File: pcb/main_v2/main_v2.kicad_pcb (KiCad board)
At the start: 4 copper layers, 68.5 x 135.2 mm, 97 parts, among them IC201 AP22811AW5-7, IC301 SE2576L-R, IC302 RMS-30+, IC401 RMS-30+, IC402 HMC374, IC501 SPF5043Z, IC502 PD0922J5050S2HF, IC503 SPF5043Z, J102 Conn_02x06_Odd_Even, J201 USB_A, J301 Conn_Coaxial, J302 Conn_Coaxial, J401 Conn_Coaxial, J402 Conn_Coaxial, SW201 SW_DIP_x01, U201 LT3042xMSE, U501 XMB0220K1-50100G, Y501 ASGTX-P-1.500GHZ-1

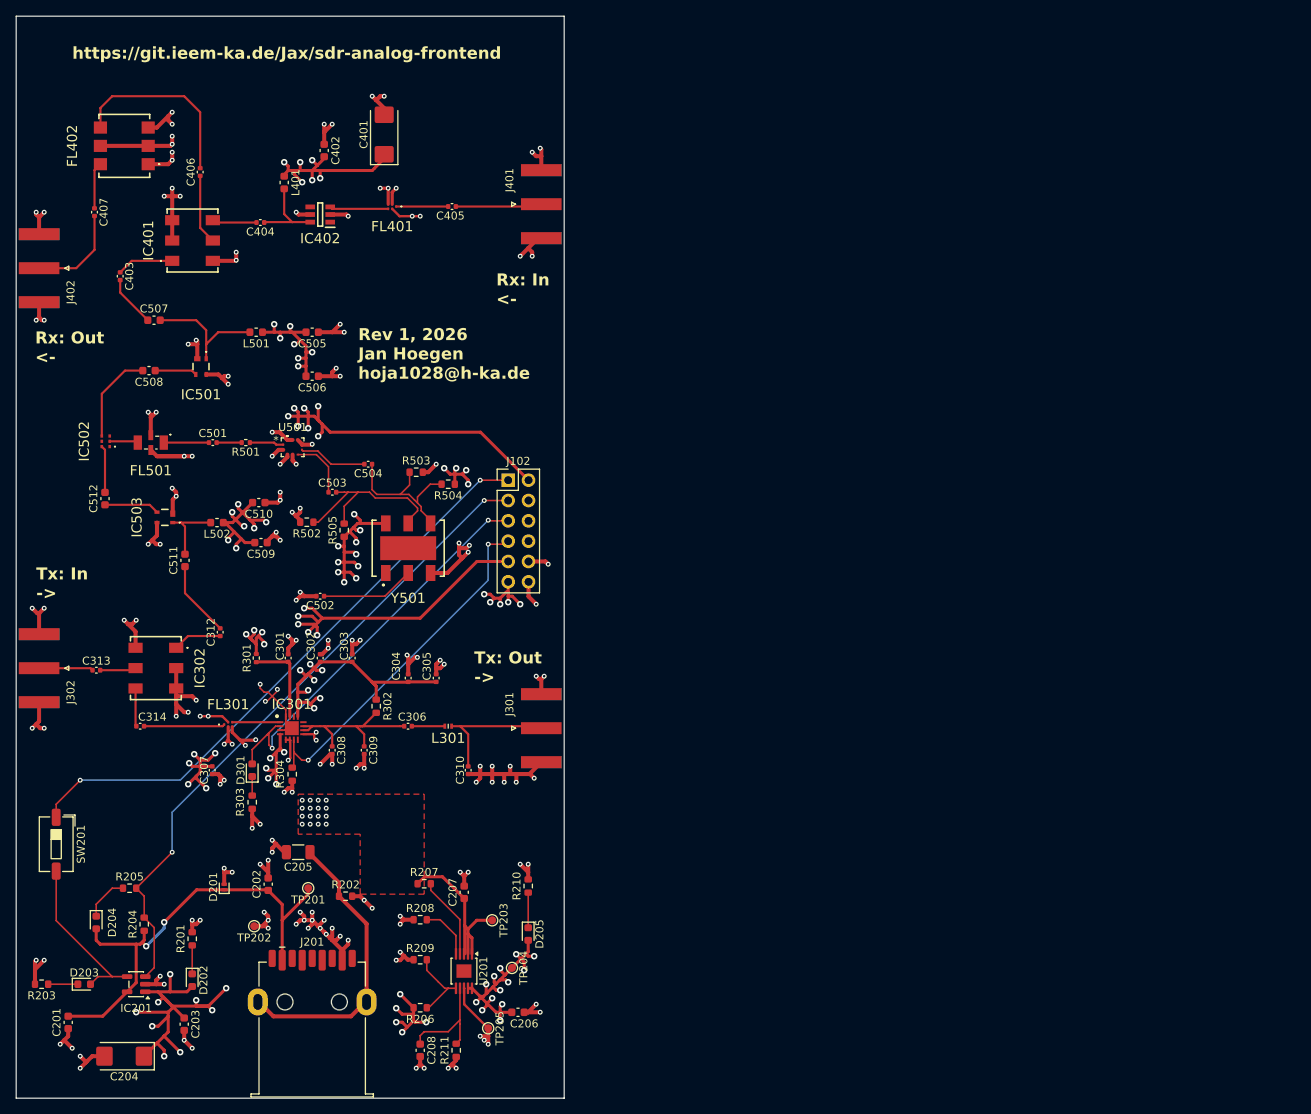
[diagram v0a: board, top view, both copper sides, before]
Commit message: added power budget
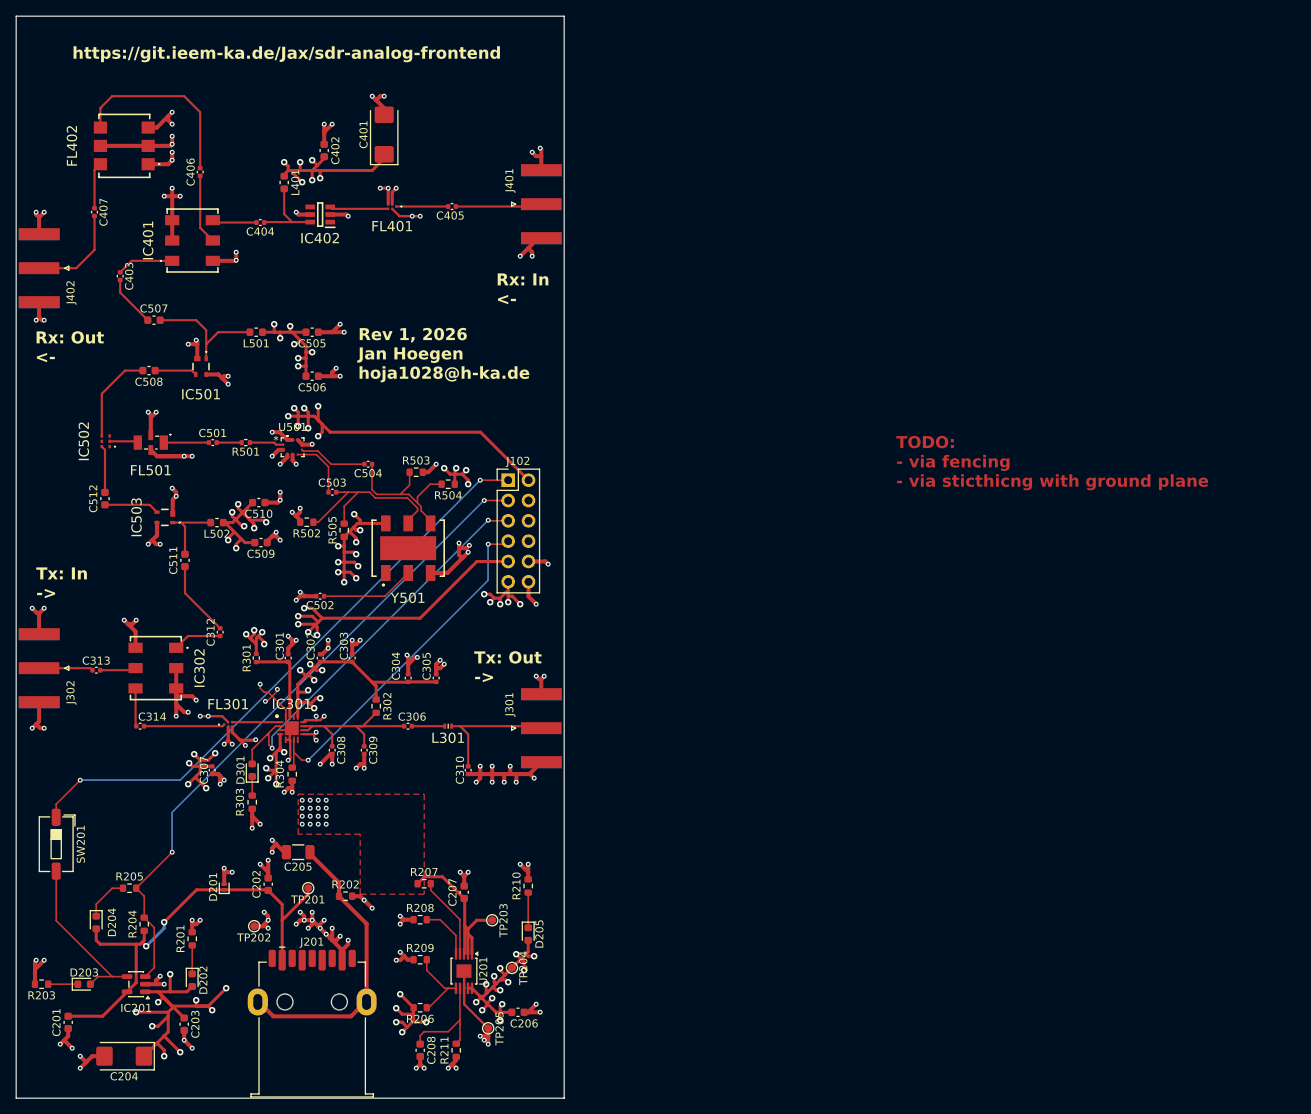
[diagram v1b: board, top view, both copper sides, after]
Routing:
- net GND: track 342.7 -> 349.6 mm, vias 168 -> 170
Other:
- board text added: "TODO: - via fencing - via sticthicng with ground plane"
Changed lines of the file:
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@@
 		(capping no)
 		(filling no)
+		(zone_defaults)
 		(pcbplotparams
 			(layerselection 0x00000000_00000000_55555555_57555501)
@@
 		(layer "Edge.Cuts")
 	)
+	(gr_text "TODO:\n- via fencing\n- via sticthicng with ground plane\n"
+		(at 183.5 116 0)
+		(layer "F.Cu")
+		(effects
+			(font
+				(size 1.5 1.5)
+				(thickness 0.3)
+				(bold yes)
+			)
+			(justify left bottom)
+		)
+	)
 	(gr_text "Rx: Out\n<-"
 		(at 75.8625 100.5 0)
@@
 	)
 	(segment
+		(start 111 145)
+		(end 111 144.5)
+		(width 0.3)
+		(layer "F.Cu")
+		(net "GND")
+	)
+	(segment
 		(start 92.79 73.21)
 		(end 93 73)
@@
 	)
 	(segment
+		(start 107.95 146)
+		(end 107.7 146.25)
+		(width 0.3)
+		(layer "F.Cu")
+		(net "GND")
+	)
+	(segment
 		(start 93.5 141.03)
 		(end 93.5 142)
@@
 	)
 	(segment
+		(start 112 144.5)
+		(end 111.5 145)
+		(width 0.3)
+		(layer "F.Cu")
+		(net "GND")
+	)
+	(segment
 		(start 128.854868 124.354868)
 		(end 128.854868 123.5)
@@
 	)
 	(segment
+		(start 129.5 176.495)
+		(end 129.5 178.505)
+		(width 0.3)
+		(layer "F.Cu")
+		(net "GND")
+	)
+	(segment
 		(start 104.75 170.75)
 		(end 105 171)
@@
 	)
 	(segment
+		(start 107.7 146.25)
+		(end 107.7 147.45)
+		(width 0.3)
+		(layer "F.Cu")
+		(net "GND")
+	)
+	(segment
 		(start 93 75)
 		(end 93 74)
@@
 	)
 	(segment
+		(start 111.5 145)
+		(end 111 145)
+		(width 0.3)
+		(layer "F.Cu")
+		(net "GND")
+	)
+	(segment
 		(start 128.5 187.09)
 		(end 128.5 187.5)
@@
 	)
 	(segment
+		(start 109.4 145.25)
+		(end 109.65 145)
+		(width 0.3)
+		(layer "F.Cu")
+		(net "GND")
+	)
+	(segment
 		(start 106.5 117.5)
 		(end 106.5 116.5)
@@
 	)
 	(segment
+		(start 109.65 145)
+		(end 111 145)
+		(width 0.3)
+		(layer "F.Cu")
+		(net "GND")
+	)
+	(segment
 		(start 88.42 133.92)
 		(end 87.5 133)
@@
 	)
 	(via
+		(at 112 144.5)
+		(size 0.6096)
+		(drill 0.3048)
+		(layers "F.Cu" "B.Cu")
+		(net "GND")
+	)
+	(via
 		(at 93 72)
 		(size 0.6096)
@@
 		(size 0.6096)
 		(drill 0.3048)
+		(layers "F.Cu" "B.Cu")
+		(net "GND")
+	)
+	(via
+		(at 111 144.5)
+		(size 0.6096)
+		(drill 0.3048)
